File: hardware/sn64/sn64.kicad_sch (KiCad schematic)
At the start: 2 parts, among them J1 N64_Cartridge_Edge_50, J2 SNES_Female_Slot_62

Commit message: Complete schematic draft: FPGA, power, clock/HDMI/audio sheets; PAL HDMI; cart audio
- New child sheets attached and wired at the root: FPGA (all 381 balls,
  W25Q128JV config flash, JTAG to the USB programmer, N64 edge through
  host-gated bus switches), power (priority-muxed host/USB eFuses, TUSB320
  permission, TPS63070 5V_PRE, FPGA bucks, cartridge eFuse and monitors),
  clock/HDMI/audio (Si5351A, TPD12S016 HDMI, PCM1808 cartridge-audio ADC).
- Real pinout: fpga/constraints/sn64_board.lpf; board top routed with it,
  all five clocks pass (SNES 28.9 MHz vs 21.48 required).
- PAL HDMI 576p50 frame-locked to the PAL SNES; Si5351 CLK2 retargeted only
  while the SNES clock is stopped. Cartridge audio mixed into HDMI.
  REGION_INFO/REGION_SOURCE mailbox telemetry shown in the menu.
  tb_system runs NTSC default, PAL header, PAL key and NTSC key.
- Safety fixes: efuse_fault_n pulled up to FPGA_3V3 (a 5V_PRE divider would
  back-drive a non-hot-socket bank); cart enable pull-ups 10k -> 4.7k
  (ECP5 config-time pull-down up to 150 uA).
- Checks: ERC 0 errors; interfaces 30/30, USB 69/69, cart 20/20, FPGA 13/13,
  power 23/23, A/V 30/30, root connectivity 4/4, all negative tests caught;
  evaluate.py --mode sim passes.

Co-Authored-By: Claude Fable 5.1 <noreply@anthropic.com>
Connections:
- no-connect marks 27 -> 0
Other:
- added sheet AV clock and cartridge audio (av-clock.kicad_sch)
- added sheet FPGA (fpga.kicad_sch)
- added sheet Power (power.kicad_sch)
- sheet USB-C programmer ports: added TARGET_VREF, USB_3V3, USB_CC1, USB_CC2, USB_VBUS, jtag_tck, jtag_tdi, jtag_tdo, jtag_tms; removed none
- title: SN 64 - cartridge interfaces -> SN 64 - system schematic draft

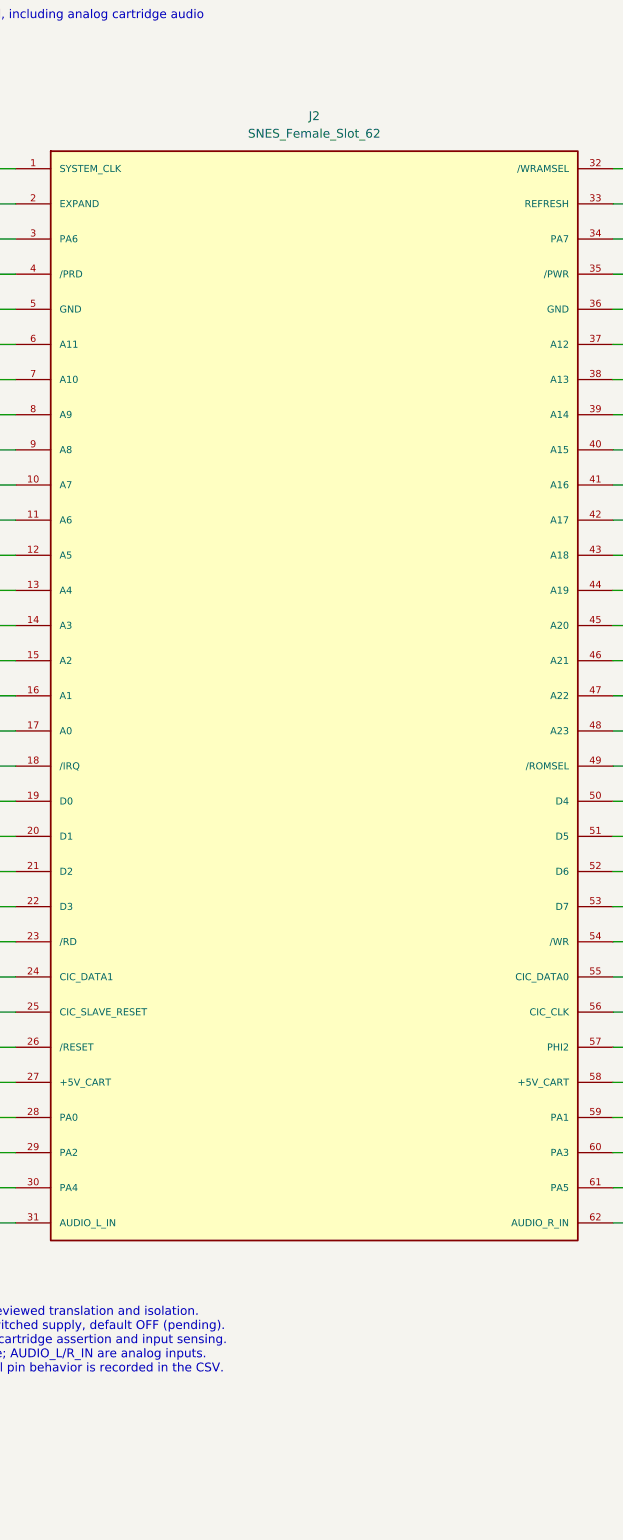
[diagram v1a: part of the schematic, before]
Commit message: Two-board split: SNES socket on its own board, joined by a 2x40 2.00 mm header
- Main root J2 becomes SN64_Socket_Joint_2x40 (pins 1-62 keep the socket
  names and wiring; 63-66 cartridge 5 V, 67-80 GND); footprint 2x40 2.00 mm
  right-angle header.
- New hardware/sn64-socket project: J1 socket on SNES_Slot_Console_7mm
  (console-replacement family, OpenSFC CartSlot geometry, 7.0 mm rows,
  ears 95 mm), J2 joint socket, two 100 nF. ERC 0/0.
- tools/split_socket_board.py (idempotent, native root edit) and
  tools/verify_socket_joint.py (9/9, negative 3/3); verify_interfaces
  understands the joint (31/31). Every other validator unchanged.
- docs: mechanical-architecture decision, dimensions lookups (OpenSFC,
  sd2snes, SNES Jr connector model, shell sizes), THIRD_PARTY OpenSFC.

Co-Authored-By: Claude Fable 5.1 <noreply@anthropic.com>
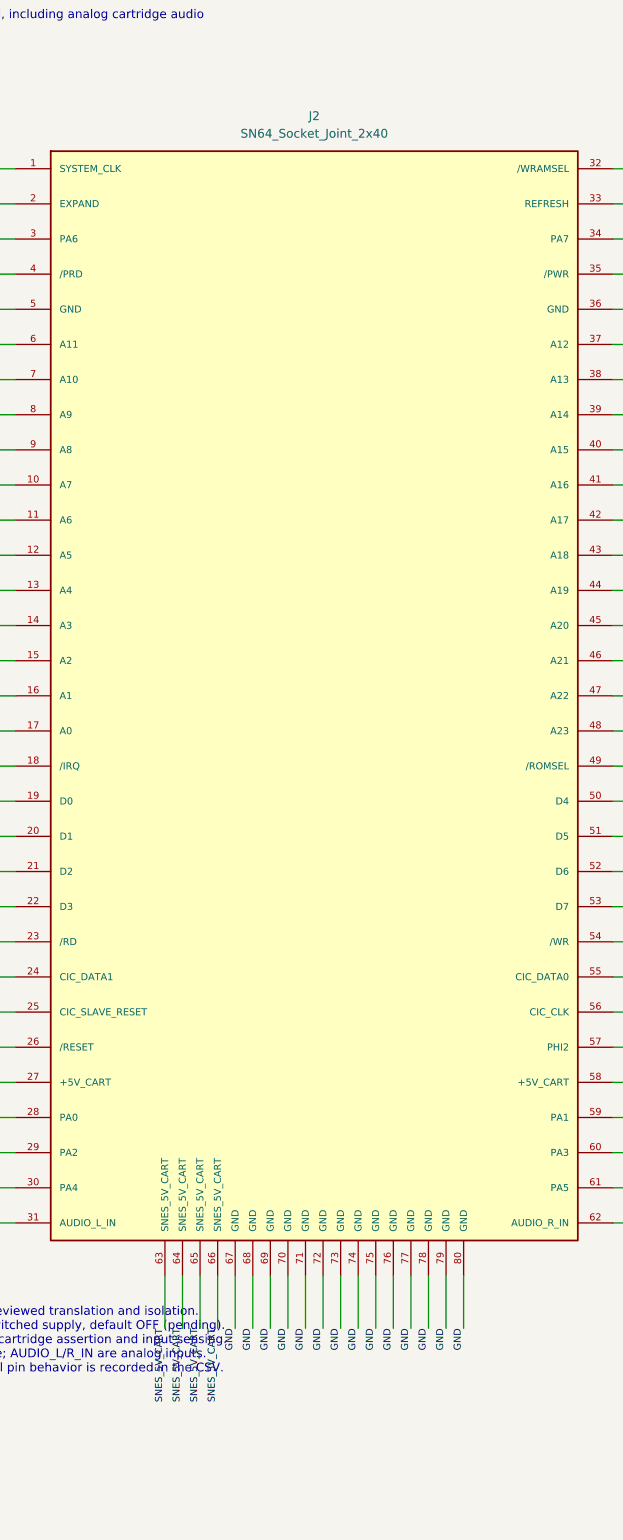
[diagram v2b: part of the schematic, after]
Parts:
- J2: value SNES_Female_Slot_62 -> SN64_Socket_Joint_2x40; footprint SN64:SNES Slot -> Connector_PinHeader_2.00mm:PinHeader_2x40_P2.00mm_Horizontal; symbol SN64:SNES_Female_Slot_62 -> SN64:SN64_Socket_Joint_2x40
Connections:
- net GND: now also J2.67 (GND), J2.68 (GND), J2.69 (GND), J2.70 (GND), J2.71 (GND), J2.72 (GND), J2.73 (GND), J2.74 (GND), J2.75 (GND), J2.76 (GND), J2.77 (GND), J2.78 (GND), J2.79 (GND), J2.80 (GND)
- net SNES_5V_CART: now also J2.63 (SNES_5V_CART), J2.64 (SNES_5V_CART), J2.65 (SNES_5V_CART), J2.66 (SNES_5V_CART)
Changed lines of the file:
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@@
 (wire (pts (xy 144.78 187.96) (xy 157.48 187.96)) (stroke (width 0) (type default)))
 (label "GND" (at 157.48 187.96 0) (effects (font (size 1.016 1.016)) (justify left bottom)))
-(symbol (lib_id "SN64:SNES_Female_Slot_62") (at 292.1 127 0) (unit 1) (exclude_from_sim no) (in_bom yes) (on_board yes) (dnp no)
+(symbol (lib_id "SN64:SN64_Socket_Joint_2x40") (at 292.1 127 0) (unit 1) (exclude_from_sim no) (in_bom yes) (on_board yes) (dnp no)
 (property "Reference" "J2" (at 292.1 43.18 0) (effects (font (size 1.27 1.27))))
-(property "Value" "SNES_Female_Slot_62" (at 292.1 45.72 0) (effects (font (size 1.27 1.27))))
-(property "Footprint" "SN64:SNES Slot" (at 292.1 127 0) (effects (font (size 1.27 1.27)) (hide yes)))
+(property "Value" "SN64_Socket_Joint_2x40" (at 292.1 45.72 0) (effects (font (size 1.27 1.27))))
+(property "Footprint" "Connector_PinHeader_2.00mm:PinHeader_2x40_P2.00mm_Horizontal" (at 292.1 127 0) (effects (font (size 1.27 1.27)) (hide yes)))
 (property "Datasheet" "" (at 292.1 127 0) (effects (font (size 1.27 1.27)) (hide yes)))
-(property "Description" "Interface draft only; see hardware/sn64/README.md" (at 292.1 127 0) (effects (font (size 1.27 1.27)) (hide yes)))
+(property "Description" "Socket-board joint (2x40 2.00 mm right-angle header); the SNES socket is J1 on hardware/sn64-socket" (at 292.1 127 0) (effects (font (size 1.27 1.27)) (hide yes)))
 (pin "1")
 (pin "2")
@@
 (pin "61")
 (pin "62")
+(pin "63")
+(pin "64")
+(pin "65")
+(pin "66")
+(pin "67")
+(pin "68")
+(pin "69")
+(pin "70")
+(pin "71")
+(pin "72")
+(pin "73")
+(pin "74")
+(pin "75")
+(pin "76")
+(pin "77")
+(pin "78")
+(pin "79")
+(pin "80")
 (instances (project "sn64" (path "/e2505a21-9627-547b-aef4-ab0d2c57bd10" (reference "J2") (unit 1)))))
 (wire (pts (xy 248.92 50.8) (xy 236.22 50.8)) (stroke (width 0) (type default)))
@@
 (label "jtag_tdo" (at 96.52 276.86 0) (effects (font (size 1.016 1.016)) (justify left bottom)))
 (label "TARGET_VREF" (at 96.52 281.94 0) (effects (font (size 1.016 1.016)) (justify left bottom)))
+(wire (pts (xy 270.51 210.82) (xy 270.51 218.44)) (stroke (width 0) (type default)))
+(label "SNES_5V_CART" (at 270.51 218.44 270) (effects (font (size 1.016 1.016)) (justify right bottom)))
+(wire (pts (xy 273.05 210.82) (xy 273.05 218.44)) (stroke (width 0) (type default)))
+(label "SNES_5V_CART" (at 273.05 218.44 270) (effects (font (size 1.016 1.016)) (justify right bottom)))
+(wire (pts (xy 275.59 210.82) (xy 275.59 218.44)) (stroke (width 0) (type default)))
+(label "SNES_5V_CART" (at 275.59 218.44 270) (effects (font (size 1.016 1.016)) (justify right bottom)))
+(wire (pts (xy 278.13 210.82) (xy 278.13 218.44)) (stroke (width 0) (type default)))
+(label "SNES_5V_CART" (at 278.13 218.44 270) (effects (font (size 1.016 1.016)) (justify right bottom)))
+(wire (pts (xy 280.67 210.82) (xy 280.67 218.44)) (stroke (width 0) (type default)))
+(label "GND" (at 280.67 218.44 270) (effects (font (size 1.016 1.016)) (justify right bottom)))
+(wire (pts (xy 283.21 210.82) (xy 283.21 218.44)) (stroke (width 0) (type default)))
+(label "GND" (at 283.21 218.44 270) (effects (font (size 1.016 1.016)) (justify right bottom)))
+(wire (pts (xy 285.75 210.82) (xy 285.75 218.44)) (stroke (width 0) (type default)))
+(label "GND" (at 285.75 218.44 270) (effects (font (size 1.016 1.016)) (justify right bottom)))
+(wire (pts (xy 288.29 210.82) (xy 288.29 218.44)) (stroke (width 0) (type default)))
+(label "GND" (at 288.29 218.44 270) (effects (font (size 1.016 1.016)) (justify right bottom)))
+(wire (pts (xy 290.83 210.82) (xy 290.83 218.44)) (stroke (width 0) (type default)))
+(label "GND" (at 290.83 218.44 270) (effects (font (size 1.016 1.016)) (justify right bottom)))
+(wire (pts (xy 293.37 210.82) (xy 293.37 218.44)) (stroke (width 0) (type default)))
+(label "GND" (at 293.37 218.44 270) (effects (font (size 1.016 1.016)) (justify right bottom)))
+(wire (pts (xy 295.91 210.82) (xy 295.91 218.44)) (stroke (width 0) (type default)))
+(label "GND" (at 295.91 218.44 270) (effects (font (size 1.016 1.016)) (justify right bottom)))
+(wire (pts (xy 298.45 210.82) (xy 298.45 218.44)) (stroke (width 0) (type default)))
+(label "GND" (at 298.45 218.44 270) (effects (font (size 1.016 1.016)) (justify right bottom)))
+(wire (pts (xy 300.99 210.82) (xy 300.99 218.44)) (stroke (width 0) (type default)))
+(label "GND" (at 300.99 218.44 270) (effects (font (size 1.016 1.016)) (justify right bottom)))
+(wire (pts (xy 303.53 210.82) (xy 303.53 218.44)) (stroke (width 0) (type default)))
+(label "GND" (at 303.53 218.44 270) (effects (font (size 1.016 1.016)) (justify right bottom)))
+(wire (pts (xy 306.07 210.82) (xy 306.07 218.44)) (stroke (width 0) (type default)))
+(label "GND" (at 306.07 218.44 270) (effects (font (size 1.016 1.016)) (justify right bottom)))
+(wire (pts (xy 308.61 210.82) (xy 308.61 218.44)) (stroke (width 0) (type default)))
+(label "GND" (at 308.61 218.44 270) (effects (font (size 1.016 1.016)) (justify right bottom)))
+(wire (pts (xy 311.15 210.82) (xy 311.15 218.44)) (stroke (width 0) (type default)))
+(label "GND" (at 311.15 218.44 270) (effects (font (size 1.016 1.016)) (justify right bottom)))
+(wire (pts (xy 313.69 210.82) (xy 313.69 218.44)) (stroke (width 0) (type default)))
+(label "GND" (at 313.69 218.44 270) (effects (font (size 1.016 1.016)) (justify right bottom)))
 )

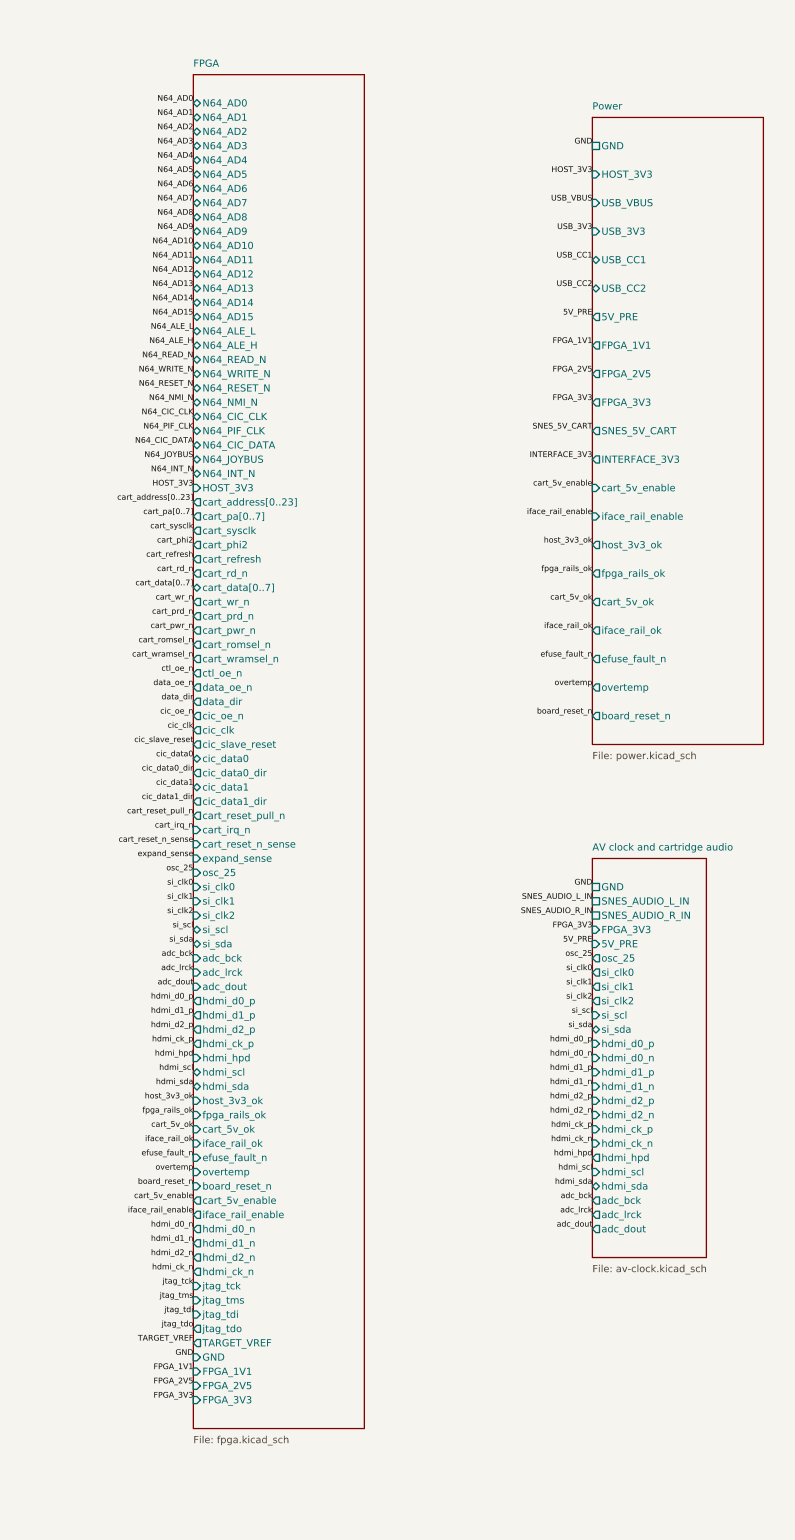
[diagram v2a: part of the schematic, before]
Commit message: Remove the on-board HDMI output: the console's own output is the only video path
Owner decision 2026-09-29: the SNES picture and sound reach the TV through the
console (M64 HDMI, N64 AV jack) via the cartridge-bus frame window; the board
has no video output of its own.

FPGA: delete sn64_av_out/av_hdmi_tx/av_serializer, tb_av_out and the vendored
hdl-util/hdmi tree; sn64_clock_init keeps CLK2 powered down (reg 3 = 0xFC) and
writes nothing after start-up; board top keeps one PLL, drops si_clk2/hdmi_*.
Sim suite 38/38; routed 203/208 DP16KD, 113 I/O, 41 % logic, all clocks pass.

Schematic: FPGA sheet rev 0.5-fpga (TMDS/HPD/DDC/si_clk2 pins removed, LPF and
CSV regenerated), A/V sheet draft 0.2-av (J701, TPD12S016, TMDS coupling, R705
gone; Si5351 pin 6 open), root sheet symbols re-packed. ERC 0 errors; all
sheet checks and negative tests pass (FPGA 14/14, A/V 27/27 with new checks).

Board: rebuilt from the new netlist (410 parts, 530 nets), FPGA-support zone
widened; DRC clean apart from the by-design USB-C edge pads and the N64 finger
mask opening. Power budget rows for the HDMI loads removed. Docs updated;
av-output-implementation.md is now the retirement record.

Co-Authored-By: Claude Fable 5.1 <noreply@anthropic.com>
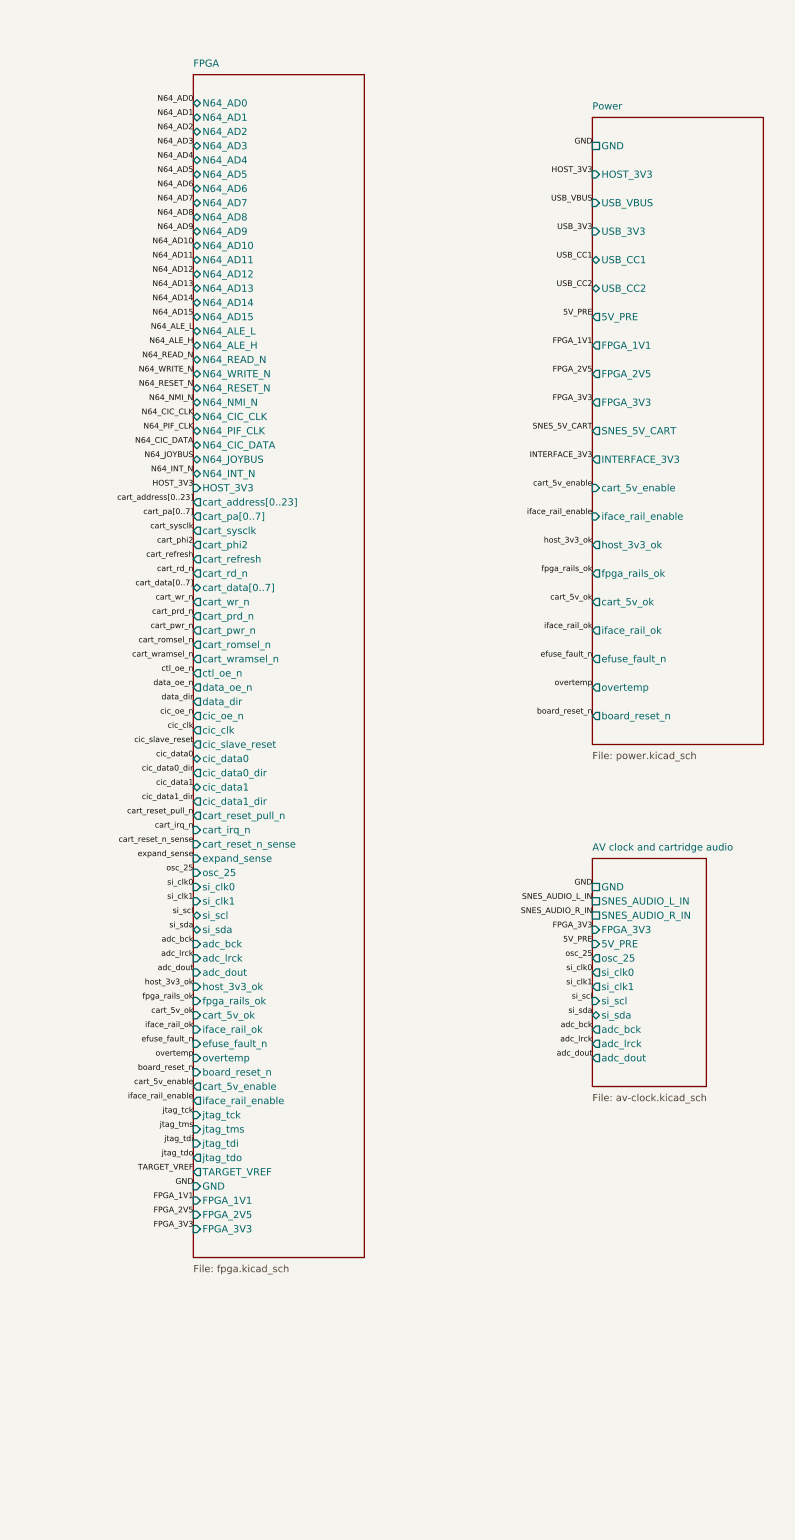
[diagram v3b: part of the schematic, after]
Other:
- sheet AV clock and cartridge audio ports: added none; removed hdmi_ck_n, hdmi_ck_p, hdmi_d0_n, hdmi_d0_p, hdmi_d1_n, hdmi_d1_p, hdmi_d2_n, hdmi_d2_p, hdmi_hpd, hdmi_scl, hdmi_sda, si_clk2
- sheet FPGA ports: added none; removed hdmi_ck_n, hdmi_ck_p, hdmi_d0_n, hdmi_d0_p, hdmi_d1_n, hdmi_d1_p, hdmi_d2_n, hdmi_d2_p, hdmi_hpd, hdmi_scl, hdmi_sda, si_clk2
